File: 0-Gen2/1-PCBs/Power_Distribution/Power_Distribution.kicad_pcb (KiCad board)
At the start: 2 copper layers, 130 x 60 mm, 38 parts, among them IC1 ACS713ELCTR-30A-T, IC2 ACS713ELCTR-30A-T, IC3 ACS713ELCTR-30A-T, IC4 ACS713ELCTR-30A-T, IC5 ACS713ELCTR-30A-T, IC6 ACS713ELCTR-30A-T, IC7 ACS713ELCTR-30A-T, IC8 ACS713ELCTR-30A-T, J1 1098169, J2 1098169, J3 Conn_01x08, J4 1986660-2, J5 Conn_01x06, J6 1098169, J7 1098169, J8 Conn_01x02, J9 Conn_01x08

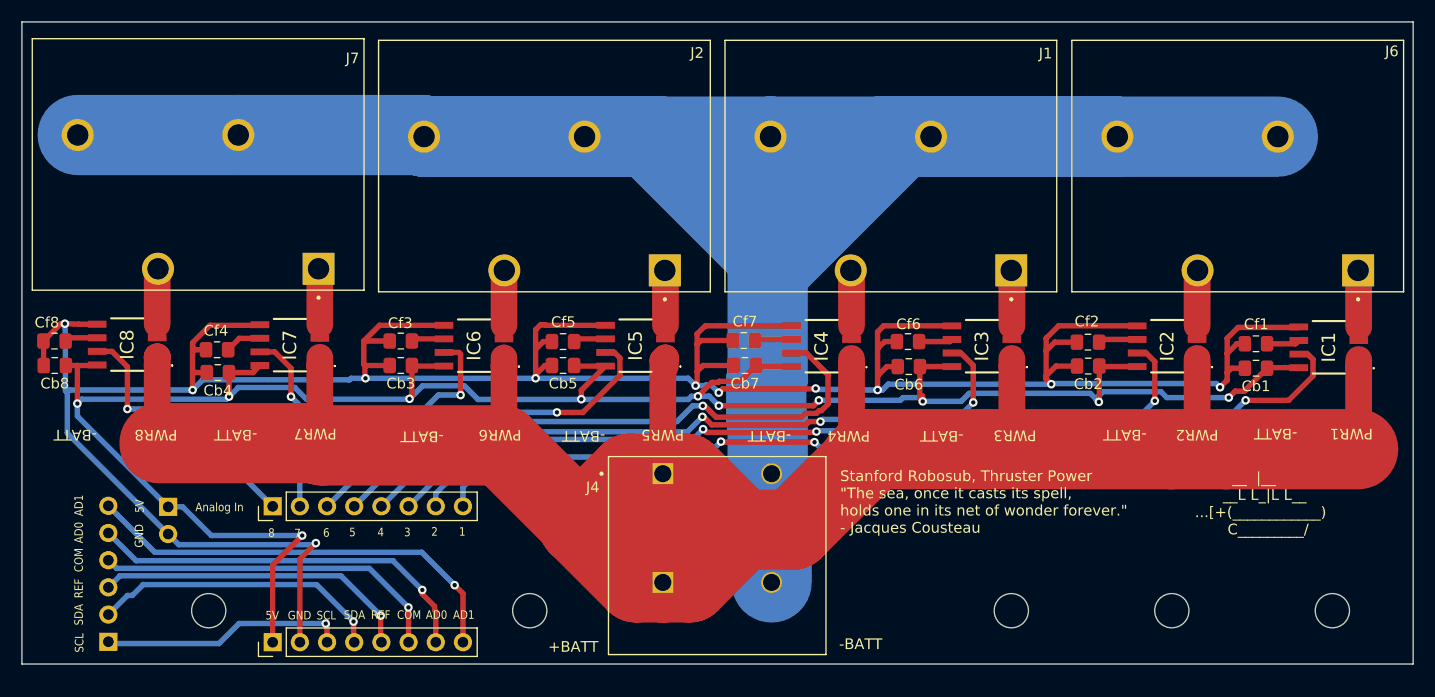
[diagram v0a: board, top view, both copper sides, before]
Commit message: [add] MLU2 progress, [bugfix] depth sensor
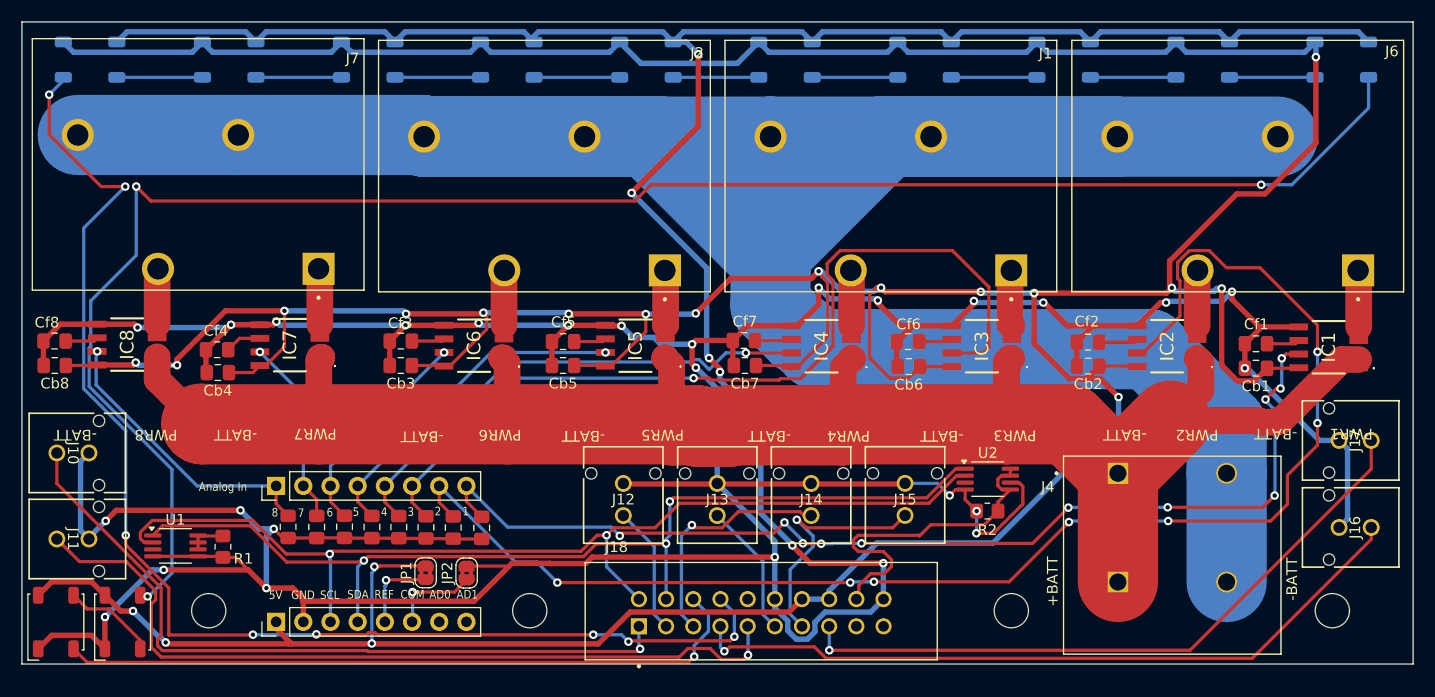
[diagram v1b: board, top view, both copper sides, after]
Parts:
- removed H1: MountingHole, MountingHole:MountingHole_3.2mm_M3
- removed J5: Conn_01x06, Connector_PinHeader_2.54mm:PinHeader_1x06_P2.54mm_Vertical
- removed J8: Conn_01x02, Connector_PinHeader_2.54mm:PinHeader_1x02_P2.54mm_Vertical
- added Cf10: 100 µF, Capacitor_SMD:C_0805_2012Metric_Pad1.18x1.45mm_HandSolder, F.Cu at (121.8, 99.5)
- added Cf11: 100 µF, Capacitor_SMD:C_0805_2012Metric_Pad1.18x1.45mm_HandSolder, F.Cu at (119.3, 99.5)
- added Cf12: 100 µF, Capacitor_SMD:C_0805_2012Metric_Pad1.18x1.45mm_HandSolder, F.Cu at (116.8, 99.5)
- added Cf13: 100 µF, Capacitor_SMD:C_0805_2012Metric_Pad1.18x1.45mm_HandSolder, F.Cu at (114.2, 99.5)
- added Cf14: 100 µF, Capacitor_SMD:C_0805_2012Metric_Pad1.18x1.45mm_HandSolder, F.Cu at (111.7, 99.5)
- added Cf15: 100 µF, Capacitor_SMD:C_0805_2012Metric_Pad1.18x1.45mm_HandSolder, F.Cu at (109.1, 99.5)
- added Cf16: 100 µF, Capacitor_SMD:C_0805_2012Metric_Pad1.18x1.45mm_HandSolder, F.Cu at (106.4, 99.5)
- added Cf9: 100 µF, Capacitor_SMD:C_0805_2012Metric_Pad1.18x1.45mm_HandSolder, F.Cu at (124.5, 99.5)
- added J10: 430450228, Imported_Footprints:CONN_SD-43045-010_02_MOL, F.Cu at (84.8, 92.5)
- added J11: 430450228, Imported_Footprints:CONN_SD-43045-010_02_MOL, F.Cu at (84.8, 100.6)
- added J12: 430450228, Imported_Footprints:CONN_SD-43045-010_02_MOL, F.Cu at (137.7, 98.4)
- added J13: 430450228, Imported_Footprints:CONN_SD-43045-010_02_MOL, F.Cu at (146.5, 98.4)
- added J14: 430450228, Imported_Footprints:CONN_SD-43045-010_02_MOL, F.Cu at (155.3, 98.4)
- added J15: 430450228, Imported_Footprints:CONN_SD-43045-010_02_MOL, F.Cu at (164.1, 98.4)
- added J16: 430450228, Imported_Footprints:CONN_SD-43045-010_02_MOL, F.Cu at (207.6, 99.5)
- added J17: 430450228, Imported_Footprints:CONN_SD-43045-010_02_MOL, F.Cu at (207.6, 91.4)
- added J18: SBH11-PBPC-D10-ST-BK, Imported_Footprints:SULLINS_SBH11-PBPC-D10-ST-BK, F.Cu at (150.6, 107.5)
- added JP1: Jumper_2_Bridged, Jumper:SolderJumper-2_P1.3mm_Bridged2Bar_RoundedPad1.0x1.5mm, F.Cu at (119.3, 103.8)
- added JP2: Jumper_2_Bridged, Jumper:SolderJumper-2_P1.3mm_Bridged2Bar_RoundedPad1.0x1.5mm, F.Cu at (123.1, 103.8)
- added LED1: 1655, LED_SMD:LED_LiteOn_LTST-E563C_PLCC4_5.0x5.0mm_P3.2mm_HandSoldering, F.Cu at (84.7, 108.3)
- added LED10: 1655, LED_SMD:LED_LiteOn_LTST-E563C_PLCC4_5.0x5.0mm_P3.2mm_HandSoldering, B.Cu at (113.9, 55.8)
- added LED11: 1655, LED_SMD:LED_LiteOn_LTST-E563C_PLCC4_5.0x5.0mm_P3.2mm_HandSoldering, B.Cu at (100.9, 55.8)
- added LED12: 1655, LED_SMD:LED_LiteOn_LTST-E563C_PLCC4_5.0x5.0mm_P3.2mm_HandSoldering, B.Cu at (87.9, 55.8)
- added LED2: 1655, LED_SMD:LED_LiteOn_LTST-E563C_PLCC4_5.0x5.0mm_P3.2mm_HandSoldering, F.Cu at (90.9, 108.3)
- added LED3: 1655, LED_SMD:LED_LiteOn_LTST-E563C_PLCC4_5.0x5.0mm_P3.2mm_HandSoldering, B.Cu at (204.9, 55.8)
- added LED4: 1655, LED_SMD:LED_LiteOn_LTST-E563C_PLCC4_5.0x5.0mm_P3.2mm_HandSoldering, B.Cu at (191.9, 55.8)
- added LED5: 1655, LED_SMD:LED_LiteOn_LTST-E563C_PLCC4_5.0x5.0mm_P3.2mm_HandSoldering, B.Cu at (178.9, 55.8)
- added LED6: 1655, LED_SMD:LED_LiteOn_LTST-E563C_PLCC4_5.0x5.0mm_P3.2mm_HandSoldering, B.Cu at (165.9, 55.8)
- added LED7: 1655, LED_SMD:LED_LiteOn_LTST-E563C_PLCC4_5.0x5.0mm_P3.2mm_HandSoldering, B.Cu at (152.9, 55.8)
- added LED8: 1655, LED_SMD:LED_LiteOn_LTST-E563C_PLCC4_5.0x5.0mm_P3.2mm_HandSoldering, B.Cu at (139.9, 55.8)
- added LED9: 1655, LED_SMD:LED_LiteOn_LTST-E563C_PLCC4_5.0x5.0mm_P3.2mm_HandSoldering, B.Cu at (126.9, 55.8)
- added R1: 10k, Resistor_SMD:R_0805_2012Metric_Pad1.20x1.40mm_HandSolder, F.Cu at (100.3, 101.3)
- added R2: 10k, Resistor_SMD:R_0805_2012Metric_Pad1.20x1.40mm_HandSolder, F.Cu at (171.8, 98.0)
- added U1: MCP9808_MSOP, Package_SO:MSOP-8_3x3mm_P0.65mm, F.Cu at (95.9, 101.2)
- added U2: MCP9808_MSOP, Package_SO:MSOP-8_3x3mm_P0.65mm, F.Cu at (171.8, 95.0)
- moved J4 42.5 mm to (183.9, 94.5)
- moved J3 1.93 mm to (105.3, 108.3)
- moved J9 1.93 mm to (105.3, 95.6)
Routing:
- net GND: track 284.8 -> 612.7 mm, vias 11 -> 32
- net 5V: track 207.1 -> 492.0 mm, vias 11 -> 20
- net Net-(LED2-DOUT): track 0.00 -> 167.2 mm, vias 0 -> 3
- net NEO_DRIVE_OUT: track 0.00 -> 119.1 mm, vias 0 -> 8
- net PWM4: track 0.00 -> 76.4 mm, vias 0 -> 1
- net SCL: track 22.7 -> 97.4 mm, vias 1 -> 2
- net PWM0: track 0.00 -> 69.8 mm, vias 0 -> 1
- net PWM3: track 0.00 -> 69.3 mm, vias 0 -> 1
- net +BATT: track 241.0 -> 172.9 mm
- net SDA: track 27.4 -> 94.6 mm, vias 1 -> 3
- net NEO_DRIVE_IN: track 0.00 -> 65.3 mm, vias 0 -> 1
- net PWM7: track 0.00 -> 62.6 mm, vias 0 -> 1
- net VIout2: track 77.9 -> 133.7 mm, vias 3 -> 7
- net AD1: track 41.1 -> 0.00 mm, vias 1 -> 0
- net AD0: track 36.9 -> 0.00 mm, vias 1 -> 0
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
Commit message: [add] silkscreen modifications to power distribution
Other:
- board text added: "Stanford Robosub '25, Thruster Power"
- board text added: "{dblquote}Survival is the ability to swim in strange water{dblquote} - Frank Herbert"
- board text added: "{dblquote}The sea, once it casts its spell, holds one in its net of wonder forever.{dblquote} - Jacques Cousteau"
- board text removed: "Stanford Robosub, Thruster Power {dblquote}The sea, once it casts its spell, holds one in its net of wonder forever.{dblquote} - Jacques Cousteau"
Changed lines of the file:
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@@
 		)
 		(fp_text user "${REFERENCE}"
-			(at 0 8.89 360)
+			(at 0 8.89 0)
 			(layer "F.Fab")
 			(effects
@@
 		(tags "resistor handsolder")
 		(property "Reference" "R2"
-			(at 0 -1.77 360)
+			(at 0 -1.77 0)
 			(layer "F.SilkS")
 			(effects
@@
 		)
 		(property "Value" "10k"
-			(at -3.41 0 360)
+			(at -3.41 0 0)
 			(layer "F.Fab")
 			(effects
@@
 		)
 		(fp_text user "${REFERENCE}"
-			(at 0 0 360)
+			(at 0 0 0)
 			(layer "F.Fab")
 			(effects
@@
 		)
 		(fp_text user "${REFERENCE}"
-			(at 0 8.89 360)
+			(at 0 8.89 0)
 			(layer "F.Fab")
 			(effects
@@
 	)
 	(gr_text "         __  |__\n       __L L_|L L__\n ...[+(____________)\n        C_________/"
-		(at 122.99 103.97 -0)
+		(at 128.27 105.4354 0)
 		(layer "B.SilkS")
 		(effects
 			(font
-				(size 1 1)
+				(size 1.4 1.4)
 				(thickness 0.15)
 			)
@@
 		)
 	)
-	(gr_text "Stanford Robosub, Thruster Power\n{dblquote}The sea, once it casts its spell, \nholds one in its net of wonder forever.{dblquote} \n- Jacques Cousteau\n"
-		(at 158.15 88.02 -0)
+	(gr_text "{dblquote}Survival is the ability to swim in strange water{dblquote} \n- Frank Herbert\n"
+		(at 157.6324 93.5736 0)
 		(layer "B.SilkS")
 		(effects
 			(font
-				(size 1 1)
-				(thickness 0.15)
+				(size 2 2)
+				(thickness 0.3)
+			)
+			(justify left bottom mirror)
+		)
+	)
+	(gr_text "{dblquote}The sea, once it casts its spell, \nholds one in its net of wonder forever.{dblquote} \n- Jacques Cousteau\n"
+		(at 209.4738 88.392 0)
+		(layer "B.SilkS")
+		(effects
+			(font
+				(size 2 2)
+				(thickness 0.3)
+			)
+			(justify left bottom mirror)
+		)
+	)
+	(gr_text "Stanford Robosub '25, Thruster Power"
+		(at 173.1264 72.898 0)
+		(layer "B.SilkS")
+		(effects
+			(font
+				(size 2 2)
+				(thickness 0.3)
 			)
 			(justify left bottom mirror)

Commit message: almost done with all orders
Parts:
- removed H2 (x2), H3, H4: MountingHole, MountingHole:MountingHole_3.2mm_M3
- added JP3: Jumper_3_Bridged12, Jumper:SolderJumper-3_P1.3mm_Bridged2Bar12_RoundedPad1.0x1.5mm, F.Cu at (128.5, 106.0)
- added R3: 2.2k Array, Imported_Footprints:RES_EXB2HV_1506x8, F.Cu at (107.9, 101.8)
- added R4: 3.9k Array, Imported_Footprints:RES_EXB2HV_1506x8, F.Cu at (111.8, 101.8)
- Cf1: value 100 µF -> 100 nF
- Cf10, Cf11, Cf12, Cf13, Cf14, Cf15, Cf16, Cf9: value 100 µF -> 1 µF
- Cf2, Cf3, Cf4, Cf5, Cf6, Cf7, Cf8: value 100 µF -> 100nF
- J4: value 1986660-2 -> Conn_01x02_Pin; footprint Imported_Footprints:TE_1986660-2 -> Connector_AMASS:AMASS_XT60IPW-M_1x03_P7.20mm_Horizontal
- moved Cf9 75.2 mm to (196.9, 79.0), turned to 180 degrees
- moved Cf10 62.8 mm to (181.2, 79.1), turned to 180 degrees
- moved Cf11 49.8 mm to (164.6, 78.8), turned to 180 degrees
- moved Cf12 35.3 mm to (146.0, 79.8)
- moved Cf16 29.9 mm to (84.6, 79.0), turned to 180 degrees
- moved Cf13 27.1 mm to (132.1, 79.1), turned to 180 degrees
- moved Cf15 22.4 mm to (99.8, 79.1), turned to 180 degrees
- moved Cf14 21.1 mm to (116.9, 79.0), turned to 180 degrees
- moved J4 7.33 mm to (191.2, 95.4), turned to 180 degrees
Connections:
- net NEO_DRIVE_IN renamed toNEO_CTRL_MOOD
- net NEO_DRIVE_OUT renamed outNEO_CTRL_MOOD
- J3 pad 1: 5V -> Net-(J3-Pin_1)
- J9 pad 1: VIout8 -> VIout8Div
- J9 pad 2: VIout7 -> VIout7Div
- J9 pad 3: VIout6 -> VIout6Div
- J9 pad 4: VIout5 -> VIout5Div
- J9 pad 5: VIout4 -> VIout4Div
- J9 pad 6: VIout3 -> VIout3Div
- J9 pad 7: VIout2 -> VIout2Div
- J9 pad 8: VIout1 -> VIout1Div
- JP1 pad 2: 5V -> +3.3V
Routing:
- net +3.3V: track 35.0 -> 96.3 mm, vias 0 -> 4
- net VIout5: track 31.7 -> 67.1 mm, vias 1 -> 4
- net GND: track 612.7 -> 644.0 mm, vias 32 -> 25
- net VIout4: track 47.3 -> 77.0 mm, vias 1 -> 6
- net VIout6: track 20.2 -> 45.5 mm, vias 1 -> 4
- net Net-(J3-Pin_1): track 0.00 -> 23.1 mm, vias 0 -> 1
- net VIout2: track 133.7 -> 112.6 mm, vias 7 -> 8
- net VIout3: track 82.5 -> 100.3 mm, vias 1 -> 4
- net VIout1: track 100.2 -> 117.7 mm, vias 11 -> 4
- net VIout8Div: track 0.00 -> 17.5 mm, vias 0 -> 1
- net VIout1Div: track 0.00 -> 16.3 mm
- net VIout3Div: track 0.00 -> 15.8 mm
- net VIout2Div: track 0.00 -> 15.6 mm, vias 0 -> 2
- net VIout6Div: track 0.00 -> 15.2 mm, vias 0 -> 1
- net VIout7Div: track 0.00 -> 15.1 mm, vias 0 -> 1
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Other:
- board text removed: "PWR1"

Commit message: ready for fab
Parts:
- added H2: MountingHole, MountingHole:MountingHole_3.2mm_M3, F.Cu at (97.8, 107.5)
- added H3: MountingHole, MountingHole:MountingHole_3.2mm_M3, F.Cu at (129.8, 107.5)
- added H4: MountingHole, MountingHole:MountingHole_3.2mm_M3, F.Cu at (177.8, 107.5)
- R3: footprint Imported_Footprints:RES_EXB2HV_1506x8 -> Imported_Footprints:2506_8x_Resistor_Array
- R4: value 3.9k Array -> 3.3k Array; footprint Imported_Footprints:RES_EXB2HV_1506x8 -> Imported_Footprints:2506_8x_Resistor_Array
- moved JP3 6.60 mm to (128.3, 99.4)
- moved J4 4.15 mm to (195.4, 95.4)
- moved R4 0.40 mm to (111.4, 101.8)
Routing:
- net 5V: track 494.7 -> 516.0 mm, vias 18 -> 20
- net GND: track 644.0 -> 659.2 mm
- net +3.3V: track 96.3 -> 102.3 mm, vias 4 -> 6
- net Net-(J3-Pin_1): track 23.1 -> 28.4 mm, vias 1 -> 3
- net VIout7Div: track 15.1 -> 10.7 mm
- net SCL: track 95.5 -> 99.9 mm
- net +BATT: track 163.7 -> 167.1 mm
- net VIout6Div: track 15.2 -> 11.9 mm
- net VIout8Div: track 17.5 -> 14.2 mm
- net outNEO_CTRL_MOOD: track 119.1 -> 116.4 mm
- net Net-(LED2-DOUT): track 167.2 -> 169.9 mm
- net -BATT: track 294.2 -> 296.0 mm
- net VIout5Div: track 12.0 -> 10.2 mm, vias 1 -> 3
- net VIout2Div: track 15.6 -> 13.9 mm, vias 2 -> 0
- net VIout1: track 117.7 -> 119.2 mm
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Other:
- board size 130 x 60 mm -> 130 x 61 mm
- board text added: "Blame: Vassili"
- board text added: "Stanford Robosub '25 Thruster Power"
- board text removed: "Stanford Robosub '25, Thruster Power"
- board text removed: "{dblquote}Survival is the ability to swim in strange water{dblquote} - Frank Herbert"
